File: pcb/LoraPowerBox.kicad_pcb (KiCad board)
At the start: 4 copper layers, 51.6 x 60.6 mm, 52 parts, among them J1 Conn_01x04_Pin, J10 Conn_01x02_Pin, J11 Conn_01x02_Pin, J12 Conn_01x05_Pin, J2 Conn_01x04_Pin, J3 Conn_01x04_Pin, J4 Conn_01x06_Pin, J5 Conn_01x04_Pin, J6 Conn_01x04_Pin, J7 Conn_01x04_Pin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

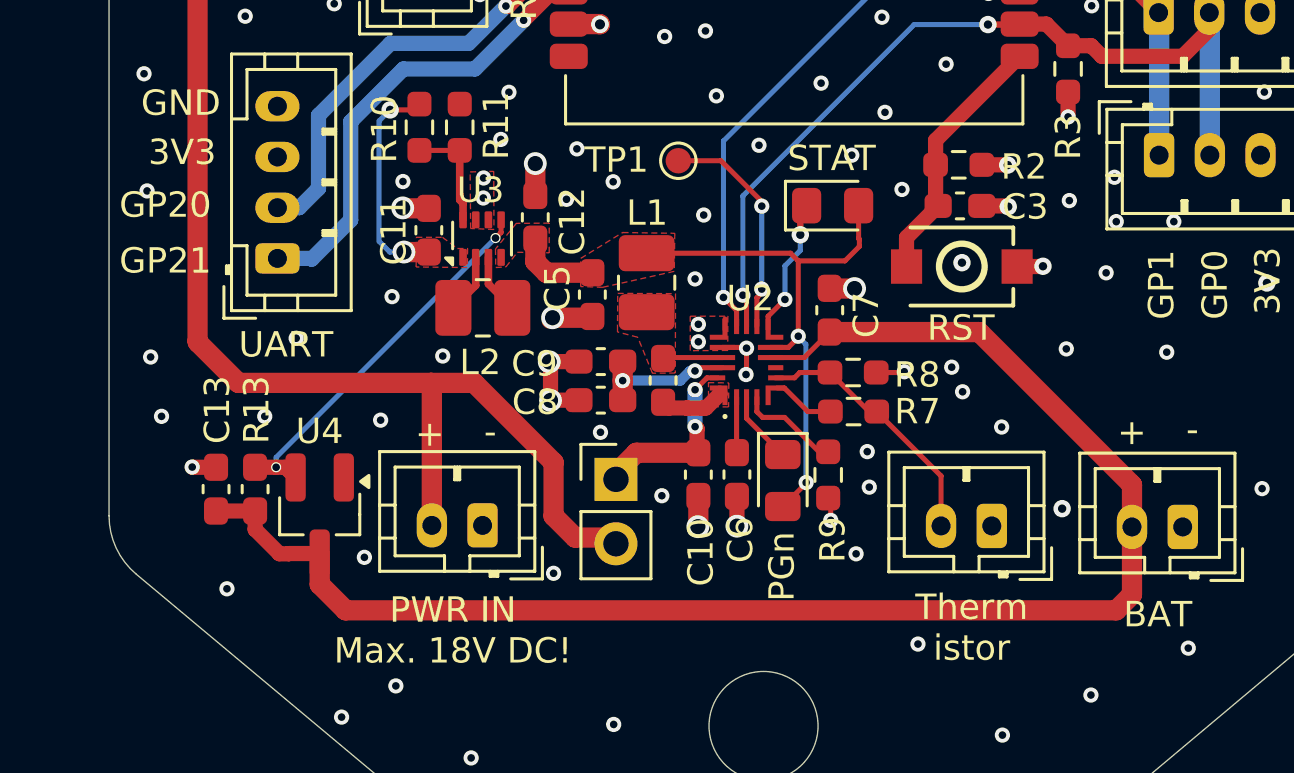
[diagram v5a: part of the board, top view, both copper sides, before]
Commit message: pcb: eye candy - move reset ic a little bit to the left
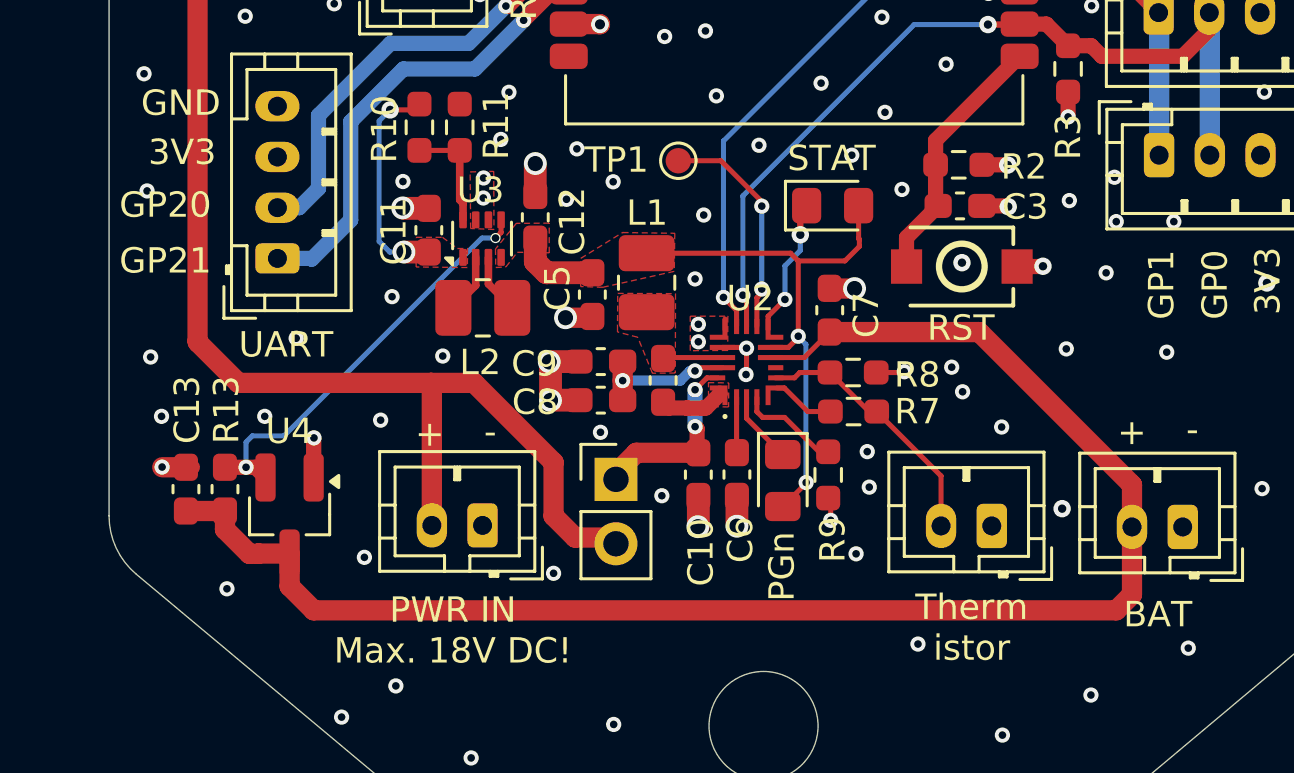
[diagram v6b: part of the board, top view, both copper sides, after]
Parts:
- moved C13 1.19 mm to (115.0, 82.2)
- moved R13 1.19 mm to (116.5, 82.2)
- moved U4 1.19 mm to (119.1, 83.3)
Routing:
- net Net-(U3-EN): track 15.2 -> 16.7 mm
- net /VBAT: track 60.6 -> 61.9 mm
- net GND: track 31.7 -> 32.5 mm, vias 155 -> 156
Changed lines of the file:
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@@
 	(footprint "Package_TO_SOT_SMD:SOT-23_Handsoldering"
 		(layer "F.Cu")
-		(at 120.2475 83.27 -90)
+		(at 119.06 83.27 -90)
 		(descr "SOT-23, Handsoldering")
 		(tags "SOT-23")
@@
 	(footprint "Capacitor_SMD:C_0603_1608Metric_Pad1.08x0.95mm_HandSolder"
 		(layer "F.Cu")
-		(at 117.7 82.23 -90)
+		(at 116.5125 82.23 -90)
 		(descr "Capacitor SMD 0603 (1608 Metric), square (rectangular) end terminal, IPC-7351 nominal with elongated pad for handsoldering. (Body size source: IPC-SM-782 page 76, https://www.pcb-3d.com/wordpress/wp-content/uploads/ipc-sm-782a_amendment_1_and_2.pdf), generated with kicad-footprint-generator")
 		(tags "capacitor handsolder")
@@
 	(footprint "Capacitor_SMD:C_0603_1608Metric_Pad1.08x0.95mm_HandSolder"
 		(layer "F.Cu")
-		(at 116.16 82.23 -90)
+		(at 114.9725 82.23 -90)
 		(descr "Capacitor SMD 0603 (1608 Metric), square (rectangular) end terminal, IPC-7351 nominal with elongated pad for handsoldering. (Body size source: IPC-SM-782 page 76, https://www.pcb-3d.com/wordpress/wp-content/uploads/ipc-sm-782a_amendment_1_and_2.pdf), generated with kicad-footprint-generator")
 		(tags "capacitor handsolder")
@@
 		(start 135.18 82.52125)
 		(end 135.18 83.69125)
-		(width 0.8)
+		(width 0.9)
 		(layer "F.Cu")
 		(net 1)
@@
 	)
 	(segment
+		(start 120.01 81.77)
+		(end 120.01 80.22)
+		(width 0.6)
+		(layer "F.Cu")
+		(net 1)
+	)
+	(segment
 		(start 131.84 45.96125)
 		(end 132.58 45.96125)
@@
 		(start 130.47 77.20125)
 		(end 129.31 77.20125)
-		(width 0.6)
+		(width 0.9)
 		(layer "F.Cu")
 		(net 1)
@@
 	)
 	(segment
-		(start 128.75 70.64875)
-		(end 128.75 69.39125)
-		(width 0.8)
-		(layer "F.Cu")
-		(net 1)
-	)
-	(segment
 		(start 129.31 77.20125)
 		(end 129.3 77.21125)
@@
 		(start 129.35 78.73125)
 		(end 129.35 77.26125)
-		(width 0.6)
+		(width 0.9)
+		(layer "F.Cu")
+		(net 1)
+	)
+	(segment
+		(start 129.94 75.47125)
+		(end 130.9225 75.47125)
+		(width 0.8)
 		(layer "F.Cu")
 		(net 1)
@@
 		(start 130.47 78.72125)
 		(end 129.36 78.72125)
-		(width 0.6)
+		(width 0.9)
 		(layer "F.Cu")
 		(net 1)
@@
 	)
 	(segment
-		(start 129.43 75.47125)
-		(end 130.9225 75.47125)
-		(width 0.8)
-		(layer "F.Cu")
-		(net 1)
-	)
-	(segment
 		(start 141.34 74.32)
 		(end 140.36875 74.32)
@@
 	)
 	(segment
+		(start 120.01 80.22)
+		(end 120.02 80.21)
+		(width 0.6)
+		(layer "F.Cu")
+		(net 1)
+	)
+	(segment
 		(start 126.11 45.13125)
 		(end 126.09 45.11125)
@@
 		(start 136.7 82.51625)
 		(end 136.7 83.69125)
-		(width 0.6)
+		(width 0.9)
 		(layer "F.Cu")
 		(net 1)
@@
 	)
 	(segment
-		(start 129.3 75.60125)
-		(end 129.43 75.47125)
-		(width 0.6)
-		(layer "F.Cu")
-		(net 1)
-	)
-	(segment
 		(start 124.55 71.1575)
 		(end 123.5375 71.1575)
-		(width 0.8)
+		(width 0.9)
 		(layer "F.Cu")
 		(net 1)
@@
 	)
 	(segment
+		(start 128.75 70.64875)
+		(end 128.75 69.39125)
+		(width 0.9)
+		(layer "F.Cu")
+		(net 1)
+	)
+	(segment
 		(start 134.07 44.21125)
 		(end 134.07 45.11125)
@@
 	)
 	(segment
-		(start 116.16 81.3675)
-		(end 115.2275 81.3675)
-		(width 0.6)
+		(start 114.9725 81.3675)
+		(end 114.04 81.3675)
+		(width 0.8)
 		(layer "F.Cu")
 		(net 1)
@@
 	)
 	(via
-		(at 115.22 81.36)
+		(at 114.0325 81.36)
 		(size 0.6)
 		(drill 0.3)
@@
 	)
 	(via
+		(at 120.02 80.21)
+		(size 0.6)
+		(drill 0.3)
+		(layers "F.Cu" "B.Cu")
+		(net 1)
+	)
+	(via
 		(at 133.85 64.38125)
 		(size 0.6)
@@
 	)
 	(via
-		(at 129.43 75.47125)
+		(at 129.94 75.47125)
 		(size 0.9)
 		(drill 0.6)
@@
 		(start 124.55 72.8825)
 		(end 123.5725 72.8825)
-		(width 0.8)
+		(width 0.9)
 		(layer "F.Cu")
 		(net 2)
@@
 		(start 129.195 73.69625)
 		(end 131 73.69625)
-		(width 0.8)
+		(width 0.9)
 		(layer "F.Cu")
 		(net 4)
@@
 		(start 128.75 72.37375)
 		(end 128.75 73.26125)
-		(width 0.8)
+		(width 0.9)
 		(layer "F.Cu")
 		(net 4)
@@
 		(start 128.75 73.26125)
 		(end 129.19 73.70125)
-		(width 0.8)
+		(width 0.9)
 		(layer "F.Cu")
 		(net 4)
@@
 	)
 	(segment
-		(start 151.66 87.01)
-		(end 152.28 86.39)
+		(start 146.255 76.03625)
+		(end 152.28 82.06125)
 		(width 0.8)
 		(layer "F.Cu")
@@
 	)
 	(segment
-		(start 146.255 76.03625)
-		(end 152.28 82.06125)
+		(start 152.28 86.39)
+		(end 151.66 87.01)
 		(width 0.8)
 		(layer "F.Cu")
@@
 	)
 	(segment
-		(start 152.28 86.39)
-		(end 152.28 83.72125)
+		(start 117.8325 84.78)
+		(end 117.8425 84.77)
 		(width 0.8)
 		(layer "F.Cu")
@@
 	)
 	(segment
-		(start 120.2475 84.77)
-		(end 120.2475 85.9875)
+		(start 114.9725 83.0925)
+		(end 116.5125 83.0925)
 		(width 0.8)
 		(layer "F.Cu")
@@
 	)
 	(segment
-		(start 119.02 84.78)
-		(end 119.03 84.77)
-		(width 0.6)
-		(layer "F.Cu")
-		(net 6)
-	)
-	(segment
-		(start 116.16 83.0925)
-		(end 117.7 83.0925)
-		(width 0.6)
+		(start 117.8425 84.77)
+		(end 119.06 84.77)
+		(width 0.8)
 		(layer "F.Cu")
 		(net 6)
 	)
 	(segment
-		(start 119.03 84.77)
-		(end 120.2475 84.77)
-		(width 0.6)
+		(start 116.5125 83.0925)
+		(end 116.5125 83.82)
+		(width 0.8)
 		(layer "F.Cu")
 		(net 6)
 	)
 	(segment
-		(start 117.7 83.0925)
-		(end 117.7 83.82)
-		(width 0.6)
+		(start 152.28 83.72125)
+		(end 152.28 86.39)
+		(width 0.8)
 		(layer "F.Cu")
 		(net 6)
 	)
 	(segment
-		(start 117.7 83.82)
-		(end 118.66 84.78)
-		(width 0.6)
+		(start 116.5125 83.82)
+		(end 117.4725 84.78)
+		(width 0.8)
 		(layer "F.Cu")
 		(net 6)
 	)
 	(segment
-		(start 120.2475 85.9875)
-		(end 121.27 87.01)
+		(start 120.01 87.01)
+		(end 119.06 86.06)
 		(width 0.8)
 		(layer "F.Cu")
@@
 	)
 	(segment
-		(start 118.66 84.78)
-		(end 119.02 84.78)
-		(width 0.6)
+		(start 119.06 86.06)
+		(end 119.06 84.77)
+		(width 0.8)
+		(layer "F.Cu")
+		(net 6)
+	)
+	(segment
+		(start 117.4725 84.78)
+		(end 117.8325 84.78)
+		(width 0.8)
 		(layer "F.Cu")
 		(net 6)
@@
 	)
 	(segment
-		(start 121.27 87.01)
-		(end 151.66 87.01)
+		(start 151.66 87.01)
+		(end 120.01 87.01)
 		(width 0.8)
 		(layer "F.Cu")
@@
 	)
 	(segment
-		(start 118.53 81.3675)
-		(end 118.895 81.3675)
+		(start 117.3425 81.3675)
+		(end 117.7075 81.3675)
 		(width 0.6)
 		(layer "F.Cu")
@@
 	)
 	(segment
-		(start 118.895 81.3675)
-		(end 119.2975 81.77)
+		(start 117.7075 81.3675)
+		(end 118.11 81.77)
 		(width 0.6)
 		(layer "F.Cu")
@@
 	)
 	(segment
-		(start 117.7 81.3675)
-		(end 118.53 81.3675)
+		(start 116.5125 81.3675)
+		(end 117.3425 81.3675)
 		(width 0.6)
 		(layer "F.Cu")
@@
 	)
 	(via
-		(at 127.18 72.33)
-		(size 0.4)
+		(at 117.3425 81.3675)
+		(size 0.6)
 		(drill 0.3)
 		(layers "F.Cu" "B.Cu")
@@
 	)
 	(via
-		(at 118.53 81.3675)
+		(at 127.18 72.33)
 		(size 0.4)
 		(drill 0.3)
@@
 	)
 	(segment
-		(start 118.53 80.98)
-		(end 118.53 81.3675)
+		(start 117.59 80.13)
+		(end 117.3425 80.3775)
+		(width 0.2)
+		(layer "B.Cu")
+		(net 43)
+	)
+	(segment
+		(start 117.3425 80.3775)
+		(end 117.3425 81.3675)
+		(width 0.2)
+		(layer "B.Cu")
+		(net 43)
+	)
+	(segment
+		(start 126.64 72.33)
+		(end 118.84 80.13)
 		(width 0.2)
 		(layer "B.Cu")
@@
 	(segment
 		(start 127.18 72.33)
-		(end 118.53 80.98)
+		(end 126.64 72.33)
+		(width 0.2)
+		(layer "B.Cu")
+		(net 43)
+	)
+	(segment
+		(start 118.84 80.13)
+		(end 117.59 80.13)
 		(width 0.2)
 		(layer "B.Cu")

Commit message: prj, pcb, sch: update to Kicad10
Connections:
- net Net-(D2-K) renamed /LED_STAT_MINUS
- net Net-(D3-K) renamed /LED_PG_MINUS

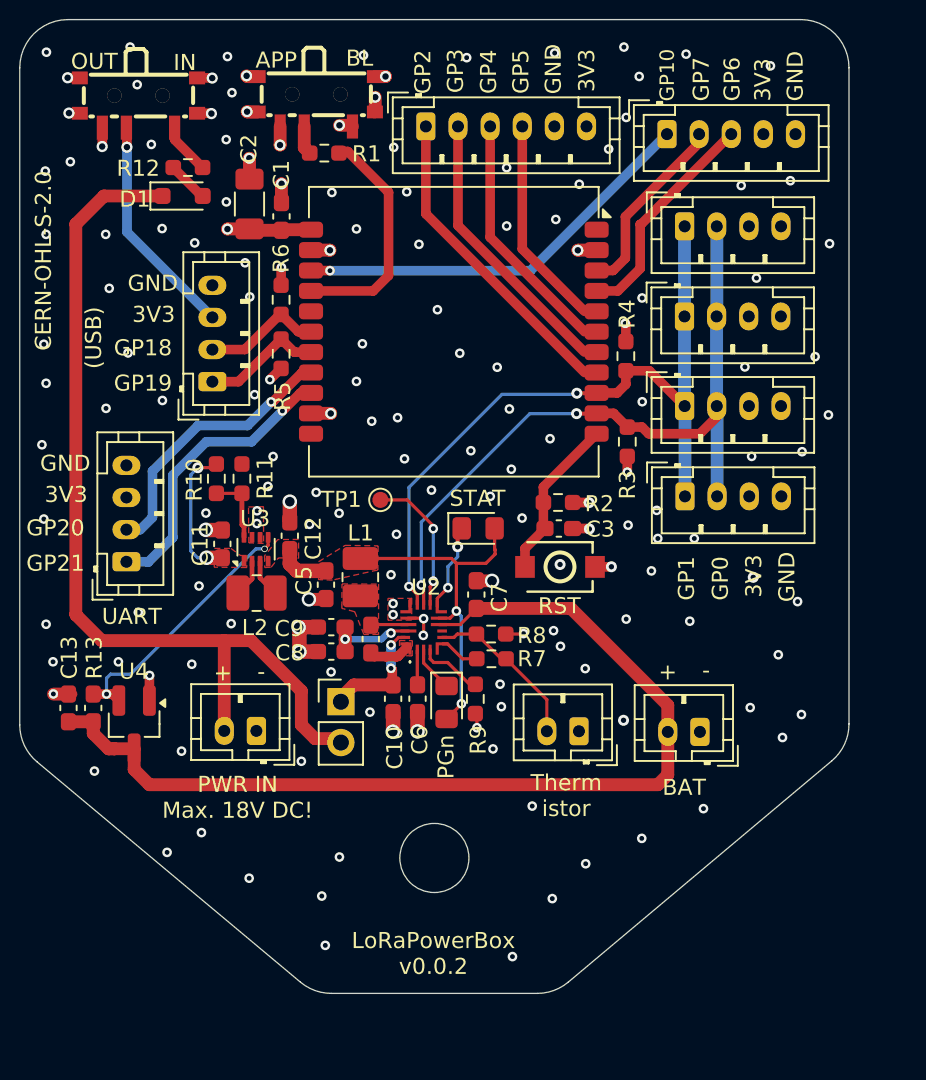
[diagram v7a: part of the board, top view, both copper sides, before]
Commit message: pcb, sch: add a resistor to the LEDs
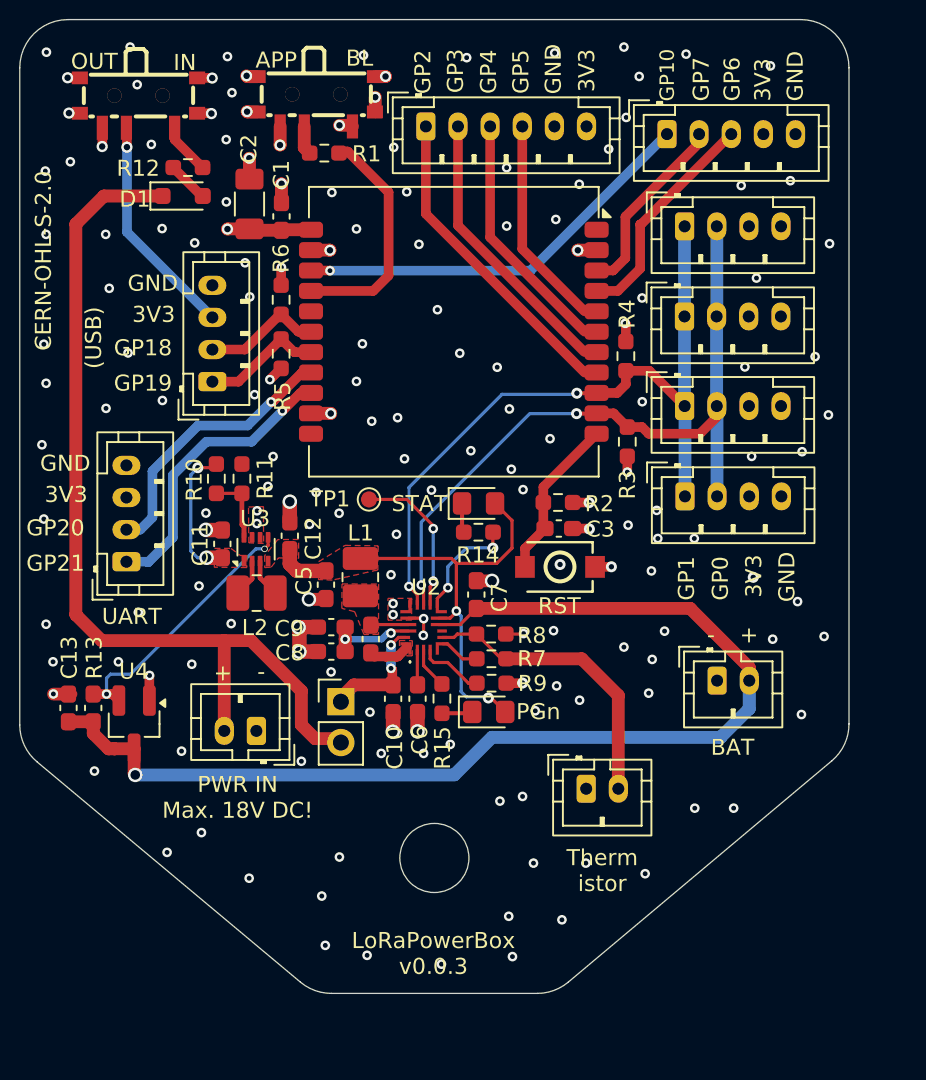
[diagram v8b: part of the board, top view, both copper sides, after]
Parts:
- added R14: 300, Resistor_SMD:R_0603_1608Metric_Pad0.98x0.95mm_HandSolder, F.Cu at (140.5, 71.3)
- added R15: 300, Resistor_SMD:R_0603_1608Metric_Pad0.98x0.95mm_HandSolder, F.Cu at (138.2, 81.7)
- moved J9 3.61 mm to (147.2, 87.3), turned to 0 degrees
- moved J10 3.37 mm to (155.3, 80.5), turned to 0 degrees
- moved D3 2.69 mm to (141.1, 82.5), turned to 0 degrees
- moved D2 1.55 mm to (140.5, 69.5)
- moved R9 1.41 mm to (141.3, 80.7), turned to 180 degrees
- moved TP1 0.71 mm to (133.7, 69.2)
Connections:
- D2 pad 1: /LED_STAT_MINUS -> Net-(D2-K)
- D3 pad 1: /LED_PG_MINUS -> Net-(D3-K)
- U2 pad 10: /LED_STAT_MINUS -> Net-(U2-STAT)
- U2 pad 3: /LED_PG_MINUS -> Net-(U2-PGn)
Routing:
- net /VBAT: track 61.9 -> 70.6 mm, vias 0 -> 1
- net Net-(J9-Pin_2): track 9.97 -> 18.1 mm
- net Net-(U2-STAT): track 0.00 -> 7.03 mm, vias 0 -> 2
- net /LED_STAT_MINUS: track 5.15 -> 0.00 mm, vias 2 -> 0
- net /SYS: track 25.2 -> 29.2 mm
- net /LED_PG_MINUS: track 2.85 -> 0.00 mm
- net Net-(U2-PGn): track 0.00 -> 2.61 mm
- net Net-(D3-K): track 0.00 -> 1.81 mm
- net Net-(D2-K): track 0.00 -> 1.69 mm
- net Net-(U2-INTn): track 8.96 -> 9.69 mm
- net GND: track 32.5 -> 32.8 mm, vias 156 -> 162
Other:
- board text added: "LoRaPowerBox v0.0.3"
- board text removed: "LoRaPowerBox v0.0.2"
